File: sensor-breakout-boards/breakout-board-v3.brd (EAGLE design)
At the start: 73.8 x 80.5 mm, 7 parts, among them X1 Sensor 1, X2 Sensor 2, X3 Sensor 3, X4 Sensor 4, X5 Multiplexer_CON1

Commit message: board complete
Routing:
- net WE1: track 0.00 -> 82.2 mm
- net RE1: track 0.00 -> 67.7 mm
- net WE2: track 0.00 -> 64.1 mm
- net WE3: track 0.00 -> 61.6 mm
- net CE1: track 0.00 -> 60.6 mm, vias 0 -> 1
- net WE4: track 0.00 -> 59.2 mm
- net RE2: track 0.00 -> 56.4 mm
- net ID: track 0.00 -> 44.4 mm
- net CE2: track 0.00 -> 44.1 mm, vias 0 -> 1
- net GND: track 0.00 -> 42.2 mm
- net RE3: track 0.00 -> 39.2 mm
- net RE4: track 0.00 -> 36.9 mm
- net D+: track 0.00 -> 36.5 mm
- net D-: track 0.00 -> 36.4 mm
- net CE3: track 0.00 -> 31.6 mm, vias 0 -> 1
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
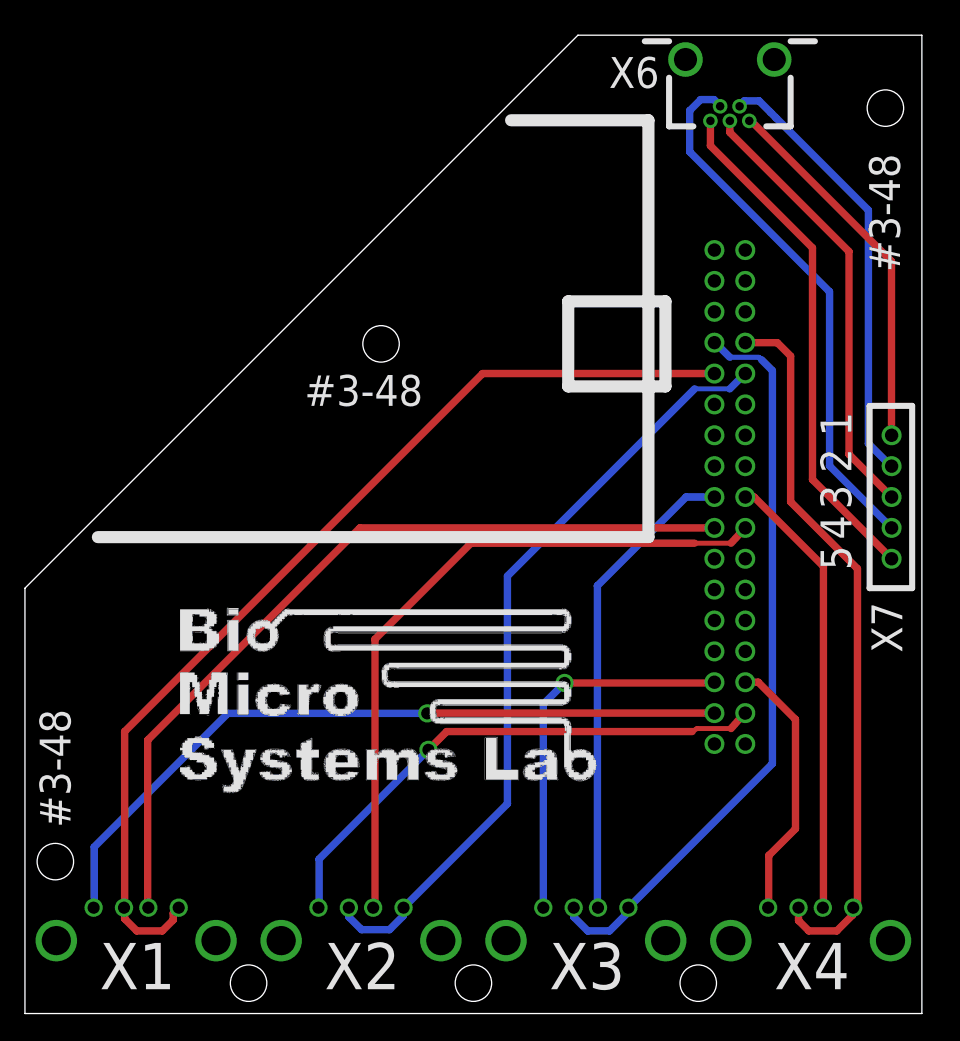
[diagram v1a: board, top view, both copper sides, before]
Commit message: added ground planes
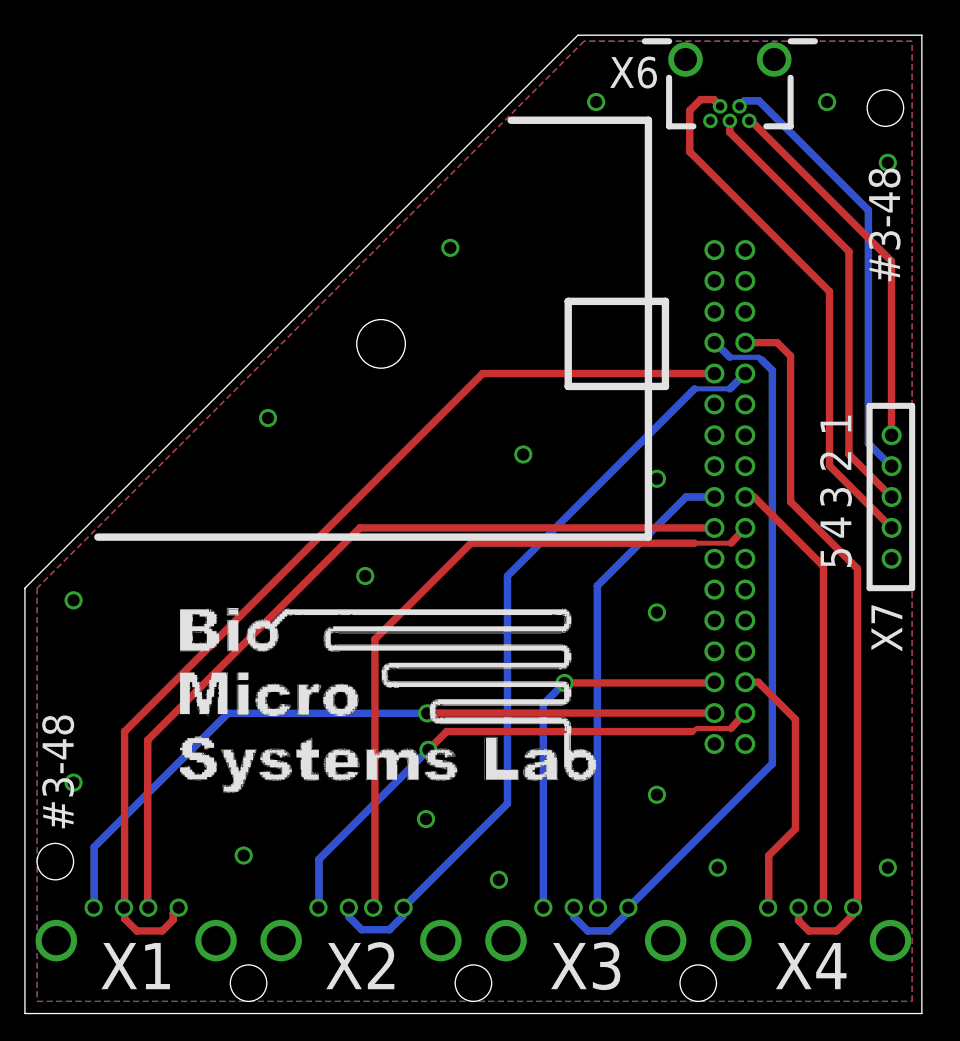
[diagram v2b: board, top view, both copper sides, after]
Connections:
- net GND: now also X5.11, X5.12, X5.23, X5.24, X5.33, X5.34
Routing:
- net GND: track 42.2 -> 0.00 mm, vias 0 -> 17
- added copper zone on layer 1, net GND
- added copper zone on layer 16, net GND
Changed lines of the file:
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@@
 <setting verticaltext="up"/>
 </settings>
-<grid distance="0.1" unitdist="mm" unit="mm" style="lines" multiple="1" display="yes" altdistance="0.025" altunitdist="inch" altunit="inch"/>
+<grid distance="1" unitdist="mm" unit="mm" style="lines" multiple="1" display="yes" altdistance="0.025" altunitdist="inch" altunit="inch"/>
 <layers>
 <layer number="1" name="Top" color="4" fill="1" visible="yes" active="yes"/>
@@
 <layer number="20" name="Dimension" color="15" fill="1" visible="yes" active="yes"/>
 <layer number="21" name="tPlace" color="7" fill="1" visible="yes" active="yes"/>
-<layer number="22" name="bPlace" color="7" fill="1" visible="no" active="yes"/>
+<layer number="22" name="bPlace" color="7" fill="1" visible="yes" active="yes"/>
 <layer number="23" name="tOrigins" color="15" fill="1" visible="yes" active="yes"/>
 <layer number="24" name="bOrigins" color="15" fill="1" visible="yes" active="yes"/>
@@
 <hole x="36.9" y="2.5" drill="3"/>
 <hole x="55.4" y="2.5" drill="3"/>
-<hole x="29.3" y="55.1" drill="3"/>
+<hole x="29.3" y="55.1" drill="4"/>
 <hole x="70.8" y="74.5" drill="3"/>
 <hole x="2.5" y="12.5" drill="3"/>
 <wire x1="0" y1="35" x2="45.5" y2="80.5" width="0" layer="20"/>
 <wire x1="0" y1="0" x2="0" y2="35" width="0" layer="20"/>
-<wire x1="6" y1="39.2" x2="51.3" y2="39.2" width="1" layer="21"/>
-<wire x1="51.3" y1="39.2" x2="51.3" y2="73.5" width="1" layer="21"/>
-<wire x1="51.3" y1="73.5" x2="40" y2="73.5" width="1" layer="21"/>
-<wire x1="44.7" y1="58.6" x2="52.7" y2="58.6" width="1" layer="21"/>
-<wire x1="52.7" y1="58.6" x2="52.7" y2="51.6" width="1" layer="21"/>
-<wire x1="52.7" y1="51.6" x2="44.7" y2="51.6" width="1" layer="21"/>
-<wire x1="44.7" y1="51.6" x2="44.7" y2="58.6" width="1" layer="21"/>
-<wire x1="5" y1="4.5" x2="73" y2="4.5" width="1" layer="22"/>
-<wire x1="5" y1="4.5" x2="5" y2="14.5" width="1" layer="22"/>
-<wire x1="5" y1="14.5" x2="1" y2="14.5" width="1" layer="22"/>
-<wire x1="68.8" y1="79.5" x2="68.8" y2="69.5" width="1" layer="22"/>
-<wire x1="68.8" y1="69.5" x2="73" y2="69.5" width="1" layer="22"/>
-<wire x1="1" y1="14.5" x2="1" y2="35" width="1" layer="22"/>
-<wire x1="73" y1="4.5" x2="73" y2="69.5" width="1" layer="22"/>
+<wire x1="6" y1="39.2" x2="51.3" y2="39.2" width="0.6096" layer="21"/>
+<wire x1="51.3" y1="39.2" x2="51.3" y2="73.5" width="0.6096" layer="21"/>
+<wire x1="51.3" y1="73.5" x2="40" y2="73.5" width="0.6096" layer="21"/>
+<wire x1="44.7" y1="58.6" x2="52.7" y2="58.6" width="0.6096" layer="21"/>
+<wire x1="52.7" y1="58.6" x2="52.7" y2="51.6" width="0.6096" layer="21"/>
+<wire x1="52.7" y1="51.6" x2="44.7" y2="51.6" width="0.6096" layer="21"/>
+<wire x1="44.7" y1="51.6" x2="44.7" y2="58.6" width="0.6096" layer="21"/>
+<wire x1="5" y1="4.5" x2="73" y2="4.5" width="0.6096" layer="22"/>
+<wire x1="5" y1="4.5" x2="5" y2="14.5" width="0.6096" layer="22"/>
+<wire x1="5" y1="14.5" x2="1" y2="14.5" width="0.6096" layer="22"/>
+<wire x1="68.8" y1="79.5" x2="68.8" y2="69.5" width="0.6096" layer="22"/>
+<wire x1="68.8" y1="69.5" x2="73" y2="69.5" width="0.6096" layer="22"/>
+<wire x1="1" y1="14.5" x2="1" y2="35" width="0.6096" layer="22"/>
+<wire x1="73" y1="4.5" x2="73" y2="69.5" width="0.6096" layer="22"/>
 <wire x1="55" y1="66" x2="55" y2="45" width="1" layer="22"/>
 <wire x1="55" y1="45" x2="53" y2="45" width="1" layer="22"/>
@@
 <wire x1="61" y1="19" x2="61" y2="66" width="1" layer="22"/>
 <wire x1="61" y1="66" x2="55" y2="66" width="1" layer="22"/>
-<text x="3.75" y="15.3" size="2.54" layer="21" font="vector" rot="R90">#3-48</text>
 <wire x1="69.5" y1="50" x2="73" y2="50" width="0.5" layer="21"/>
 <wire x1="73" y1="50" x2="73" y2="35" width="0.5" layer="21"/>
@@
 <text x="68" y="41.5" size="2.54" layer="21" font="vector" rot="R90">3</text>
 <text x="68" y="39" size="2.54" layer="21" font="vector" rot="R90">4</text>
-<text x="23" y="50" size="2.54" layer="21" font="vector">#3-48</text>
-<text x="72" y="61" size="2.54" layer="21" font="vector" rot="R90">#3-48</text>
+<text x="72" y="60" size="2.54" layer="21" font="vector" rot="R90">#3-48</text>
 <rectangle x1="16.7875" y1="18.1375" x2="16.8875" y2="18.1625" layer="21"/>
 <rectangle x1="16.9625" y1="18.1375" x2="16.9875" y2="18.1625" layer="21"/>
@@
 <wire x1="53" y1="80" x2="51" y2="80" width="0.5" layer="21"/>
 <wire x1="63" y1="80" x2="65" y2="80" width="0.5" layer="21"/>
+<text x="4" y="15" size="2.54" layer="21" font="vector" rot="R90">#3-48</text>
 </plain>
 <attributes>
@@
 <contactref element="X7" pad="4"/>
 <contactref element="X6" pad="4"/>
-<wire x1="57.2" y1="74.65" x2="57.2" y2="74.7" width="0.6096" layer="16"/>
-<wire x1="57.2" y1="74.7" x2="56.7" y2="75.2" width="0.6096" layer="16"/>
-<wire x1="56.7" y1="75.2" x2="55.6" y2="75.2" width="0.6096" layer="16"/>
-<wire x1="55.6" y1="75.2" x2="54.7" y2="74.3" width="0.6096" layer="16"/>
+<wire x1="56.7" y1="75.2" x2="55.6" y2="75.2" width="0.6096" layer="1"/>
+<wire x1="55.6" y1="75.2" x2="54.7" y2="74.3" width="0.6096" layer="1"/>
 <wire x1="71.31" y1="39.96" x2="71.31" y2="39.99" width="0.6096" layer="16"/>
-<wire x1="66.2" y1="59.4" x2="54.7" y2="70.9" width="0.6096" layer="16"/>
-<wire x1="54.7" y1="70.9" x2="54.7" y2="74.3" width="0.6096" layer="16"/>
-<wire x1="66.2" y1="59.4" x2="66.2" y2="45.07" width="0.6096" layer="16"/>
-<wire x1="66.2" y1="45.07" x2="71.31" y2="39.96" width="0.6096" layer="16"/>
+<wire x1="66.2" y1="59.4" x2="54.7" y2="70.9" width="0.6096" layer="1"/>
+<wire x1="54.7" y1="70.9" x2="54.7" y2="74.3" width="0.6096" layer="1"/>
+<wire x1="66.2" y1="59.4" x2="66.2" y2="45.07" width="0.6096" layer="1"/>
+<wire x1="66.2" y1="45.07" x2="71.31" y2="39.96" width="0.6096" layer="1"/>
+<wire x1="56.7" y1="75.2" x2="56.7" y2="75.15" width="0.6096" layer="1"/>
+<wire x1="56.7" y1="75.15" x2="57.2" y2="74.65" width="0.6096" layer="1"/>
 </signal>
 <signal name="GND">
 <contactref element="X7" pad="5"/>
 <contactref element="X6" pad="5"/>
-<wire x1="56.4" y1="73.45" x2="56.4" y2="71.4" width="0.6096" layer="1"/>
-<wire x1="56.4" y1="71.4" x2="64.8" y2="63" width="0.6096" layer="1"/>
-<wire x1="64.8" y1="63" x2="64.8" y2="43.93" width="0.6096" layer="1"/>
-<wire x1="64.8" y1="43.93" x2="71.31" y2="37.42" width="0.6096" layer="1"/>
+<contactref element="X5" pad="11"/>
+<contactref element="X5" pad="33"/>
+<contactref element="X5" pad="23"/>
+<contactref element="X5" pad="12"/>
+<contactref element="X5" pad="34"/>
+<contactref element="X5" pad="24"/>
+<polygon width="0" layer="16" isolate="0.5">
+<vertex x="73" y="80"/>
+<vertex x="46" y="80"/>
+<vertex x="1" y="35"/>
+<vertex x="1" y="1"/>
+<vertex x="73" y="1"/>
+</polygon>
+<polygon width="0" layer="1" isolate="0.5">
+<vertex x="73" y="80"/>
+<vertex x="46" y="80"/>
+<vertex x="1" y="35"/>
+<vertex x="1" y="1"/>
+<vertex x="73" y="1"/>
+</polygon>
+<via x="4" y="19" extent="1-16" drill="1"/>
+<via x="4" y="34" extent="1-16" drill="1"/>
+<via x="18" y="13" extent="1-16" drill="1"/>
+<via x="33" y="16" extent="1-16" drill="1"/>
+<via x="39" y="11" extent="1-16" drill="1"/>
+<via x="52" y="18" extent="1-16" drill="1"/>
+<via x="57" y="12" extent="1-16" drill="1"/>
+<via x="71" y="12" extent="1-16" drill="1"/>
+<via x="52" y="33" extent="1-16" drill="1"/>
+<via x="28" y="36" extent="1-16" drill="1"/>
+<via x="20" y="49" extent="1-16" drill="1"/>
+<via x="41" y="46" extent="1-16" drill="1"/>
+<via x="52" y="44" extent="1-16" drill="1"/>
+<via x="35" y="63" extent="1-16" drill="1"/>
+<via x="47" y="75" extent="1-16" drill="1"/>
+<via x="66" y="75" extent="1-16" drill="1"/>
+<via x="71" y="70" extent="1-16" drill="1"/>
 </signal>
 </signals>
